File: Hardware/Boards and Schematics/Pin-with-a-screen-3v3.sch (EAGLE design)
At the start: 43 parts, among them J1 AVR_SPI_PRG_6NS, Q2 BL8530, U1 ATMEGA328P, U2 MICRO-SD-SOCKET-SMD1:1, Y1 8MHz

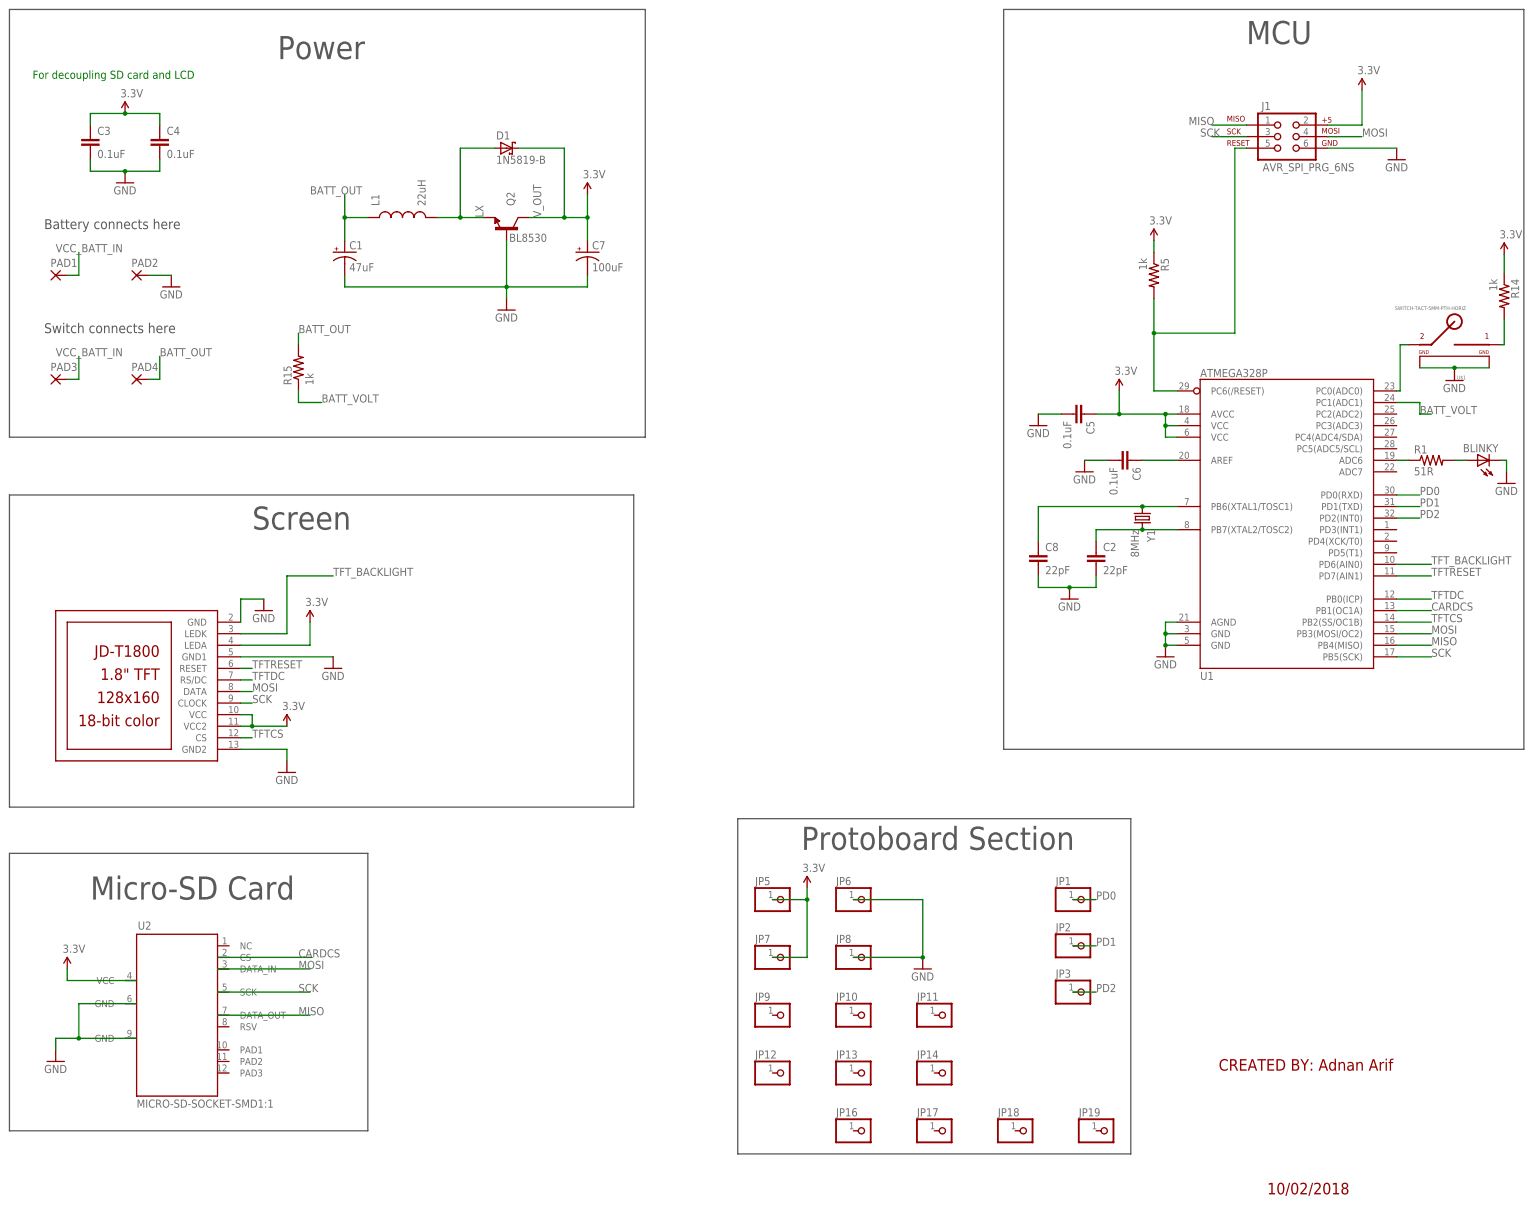
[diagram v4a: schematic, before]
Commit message: Changed switch configuration, generated gerbers
Switch now connects directly to bottom side of PCB instead of being
wired to pads. Horizontal SPDT switch selected.

New gerbers generated with Seeed Studio CAM file.
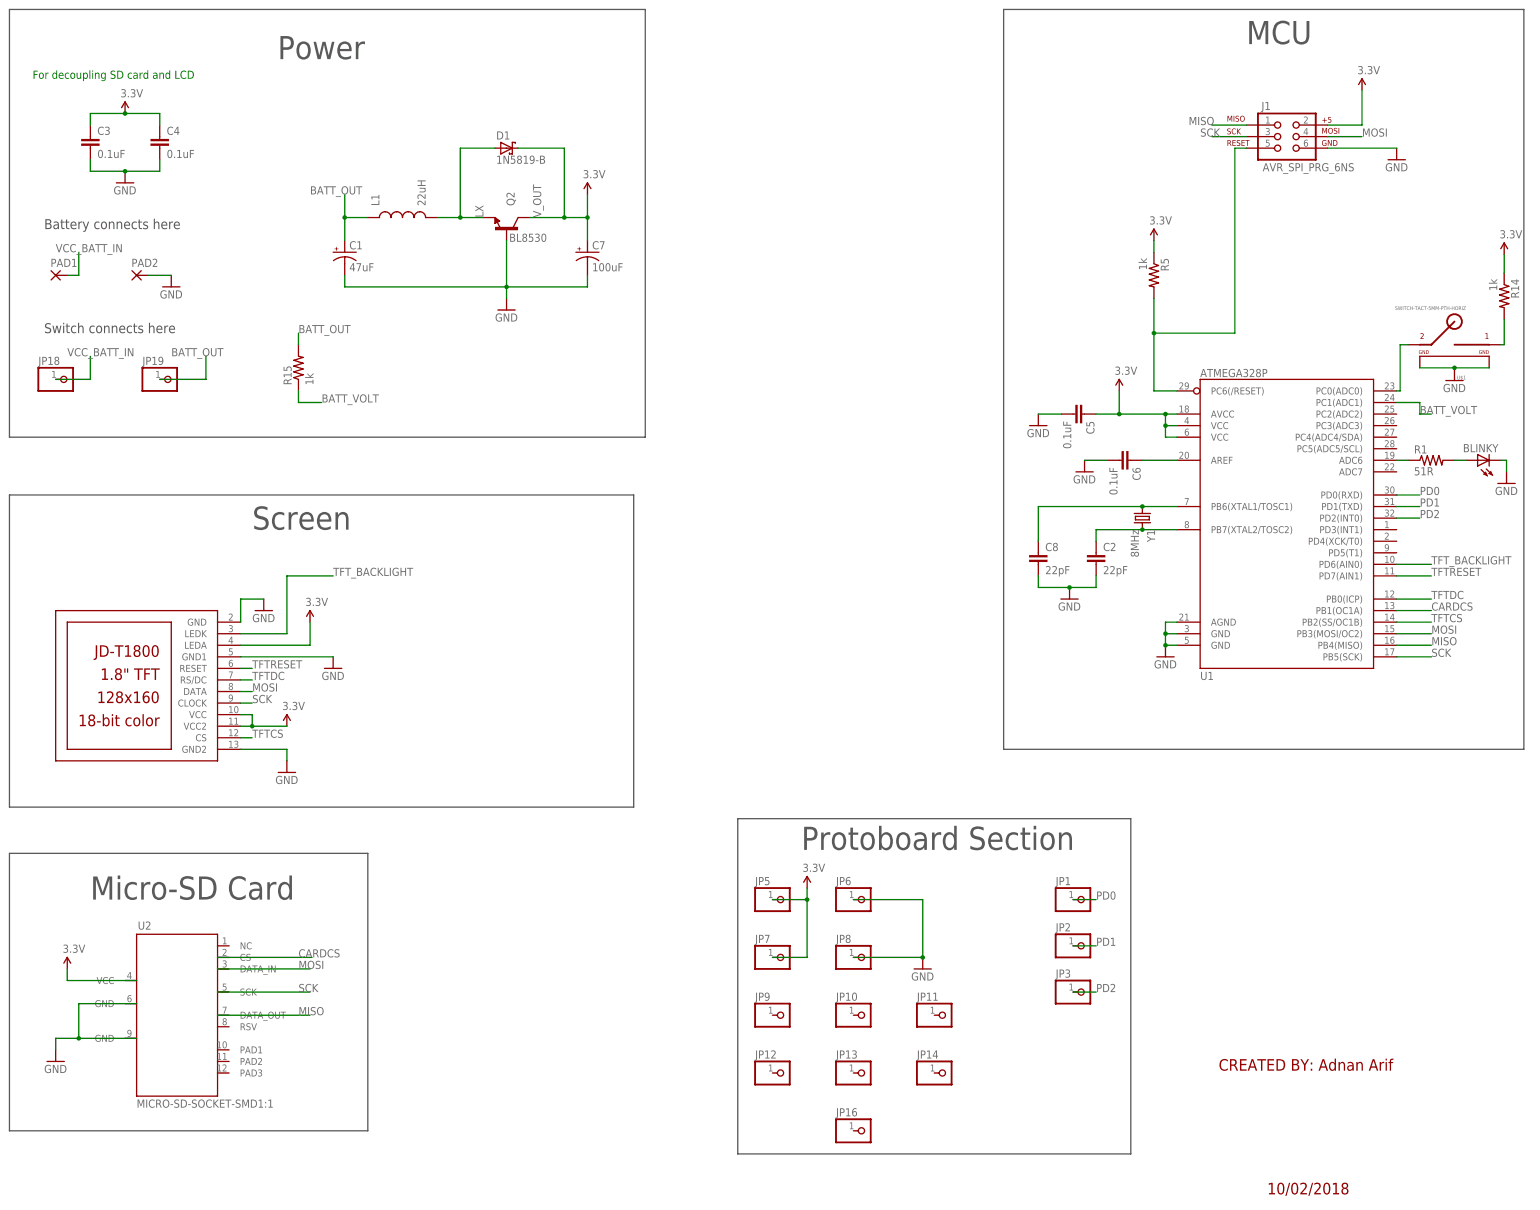
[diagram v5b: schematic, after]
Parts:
- removed JP17: (no value), pinhead:PINHD-1X1
- removed PAD3, PAD4: (no value), wirepad:2,15/1,0
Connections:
- net BATT_OUT: now also JP19.1; no longer PAD4.P
- net VCC_BATT_IN: now also JP18.1; no longer PAD3.P
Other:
- moved on the sheet: JP18, JP19
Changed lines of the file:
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@@
 <part name="PAD1" library="wirepad" deviceset="2,15/1,0" device=""/>
 <part name="PAD2" library="wirepad" deviceset="2,15/1,0" device=""/>
-<part name="PAD3" library="wirepad" deviceset="2,15/1,0" device=""/>
-<part name="PAD4" library="wirepad" deviceset="2,15/1,0" device=""/>
 <part name="GND14" library="SparkFun-Aesthetics" deviceset="GND" device=""/>
 <part name="JP5" library="pinhead" deviceset="PINHD-1X1" device=""/>
@@
 <part name="JP14" library="pinhead" deviceset="PINHD-1X1" device=""/>
 <part name="JP16" library="pinhead" deviceset="PINHD-1X1" device=""/>
-<part name="JP17" library="pinhead" deviceset="PINHD-1X1" device=""/>
 <part name="JP18" library="pinhead" deviceset="PINHD-1X1" device=""/>
 <part name="JP19" library="pinhead" deviceset="PINHD-1X1" device=""/>
@@
 <instance part="PAD1" gate="1" x="-127" y="127"/>
 <instance part="PAD2" gate="1" x="-109.22" y="127"/>
-<instance part="PAD3" gate="1" x="-127" y="104.14"/>
-<instance part="PAD4" gate="1" x="-109.22" y="104.14"/>
 <instance part="GND14" gate="1" x="-101.6" y="124.46"/>
 <instance part="JP5" gate="G$1" x="33.02" y="-10.16"/>
@@
 <instance part="JP14" gate="G$1" x="68.58" y="-48.26"/>
 <instance part="JP16" gate="G$1" x="50.8" y="-60.96"/>
-<instance part="JP17" gate="G$1" x="68.58" y="-60.96"/>
-<instance part="JP18" gate="G$1" x="86.36" y="-60.96"/>
-<instance part="JP19" gate="G$1" x="104.14" y="-60.96"/>
+<instance part="JP18" gate="G$1" x="-124.46" y="104.14"/>
+<instance part="JP19" gate="G$1" x="-101.6" y="104.14"/>
 <instance part="GND2" gate="1" x="63.5" y="-25.4"/>
 <instance part="SUPPLY10" gate="G$1" x="38.1" y="-7.62"/>
@@
 </segment>
 <segment>
-<pinref part="PAD3" gate="1" pin="P"/>
-<wire x1="-124.46" y1="104.14" x2="-121.92" y2="104.14" width="0.1524" layer="91"/>
-<wire x1="-121.92" y1="104.14" x2="-121.92" y2="109.22" width="0.1524" layer="91"/>
-<label x="-127" y="109.22" size="1.778" layer="95"/>
+<wire x1="-127" y1="104.14" x2="-119.38" y2="104.14" width="0.1524" layer="91"/>
+<wire x1="-119.38" y1="104.14" x2="-119.38" y2="109.22" width="0.1524" layer="91"/>
+<label x="-124.46" y="109.22" size="1.778" layer="95"/>
+<pinref part="JP18" gate="G$1" pin="1"/>
 </segment>
 </net>
@@
 </segment>
 <segment>
-<pinref part="PAD4" gate="1" pin="P"/>
-<wire x1="-106.68" y1="104.14" x2="-104.14" y2="104.14" width="0.1524" layer="91"/>
-<label x="-104.14" y="109.22" size="1.778" layer="95"/>
-<wire x1="-104.14" y1="104.14" x2="-104.14" y2="109.22" width="0.1524" layer="91"/>
-</segment>
-</net>
+<pinref part="JP19" gate="G$1" pin="1"/>
+<wire x1="-104.14" y1="104.14" x2="-93.98" y2="104.14" width="0.1524" layer="91"/>
+<wire x1="-93.98" y1="104.14" x2="-93.98" y2="109.22" width="0.1524" layer="91"/>
+<label x="-101.6" y="109.22" size="1.778" layer="95"/>
+</segment>
+</net>
